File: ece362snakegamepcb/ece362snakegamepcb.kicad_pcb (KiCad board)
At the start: 2 copper layers, 52 x 71.5 mm, 49 parts, among them J1 USB_B_Micro, J2 Conn_02x26_Odd_Even, J3 Conn_02x26_Odd_Even, J4 SM03B-SRSS-TB, SW1 SW_Push, SW2 SW_Push, U1 RP2350_80QFN, U2 NCP1117-3.3_SOT223, U3 W25Q128JVS, U4 DNF, Y1 ABM8-272-T3

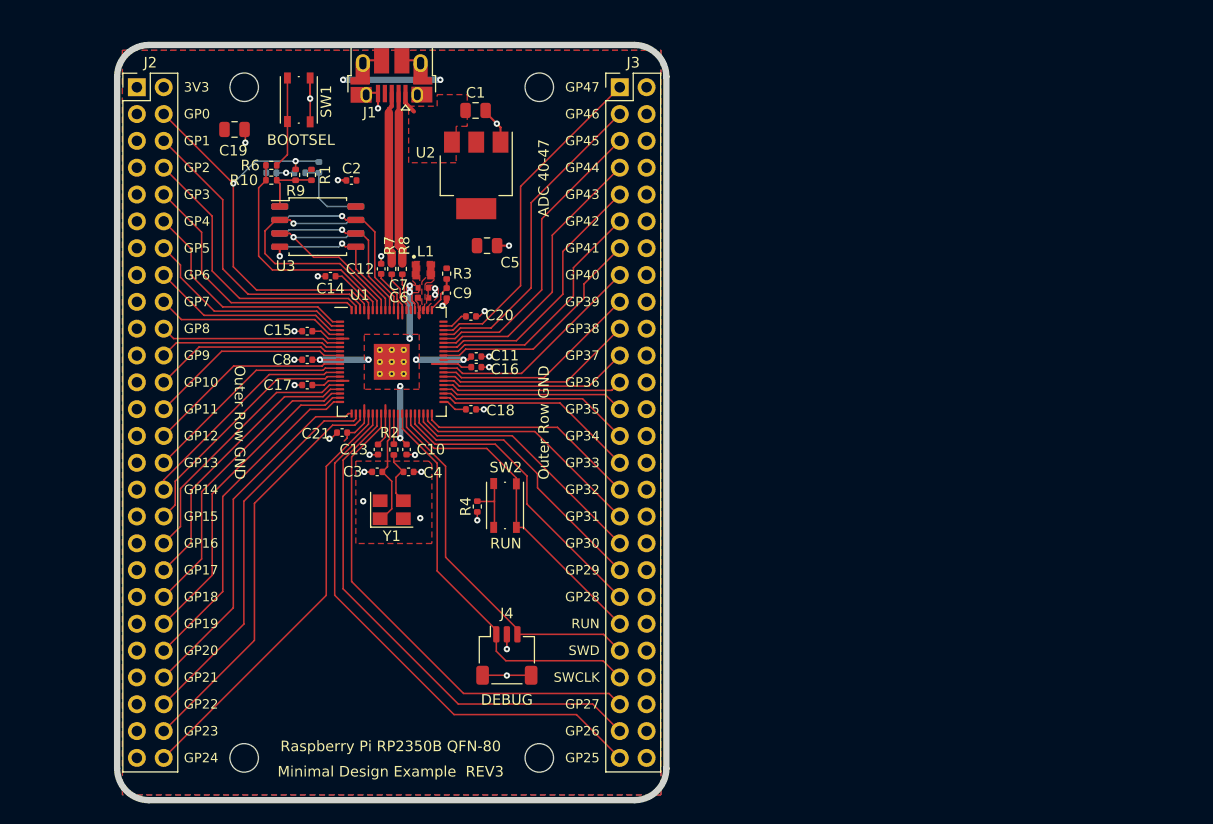
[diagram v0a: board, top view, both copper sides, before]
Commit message: Finished schematic and almost done with PCB layout. Removed autosave file and added several
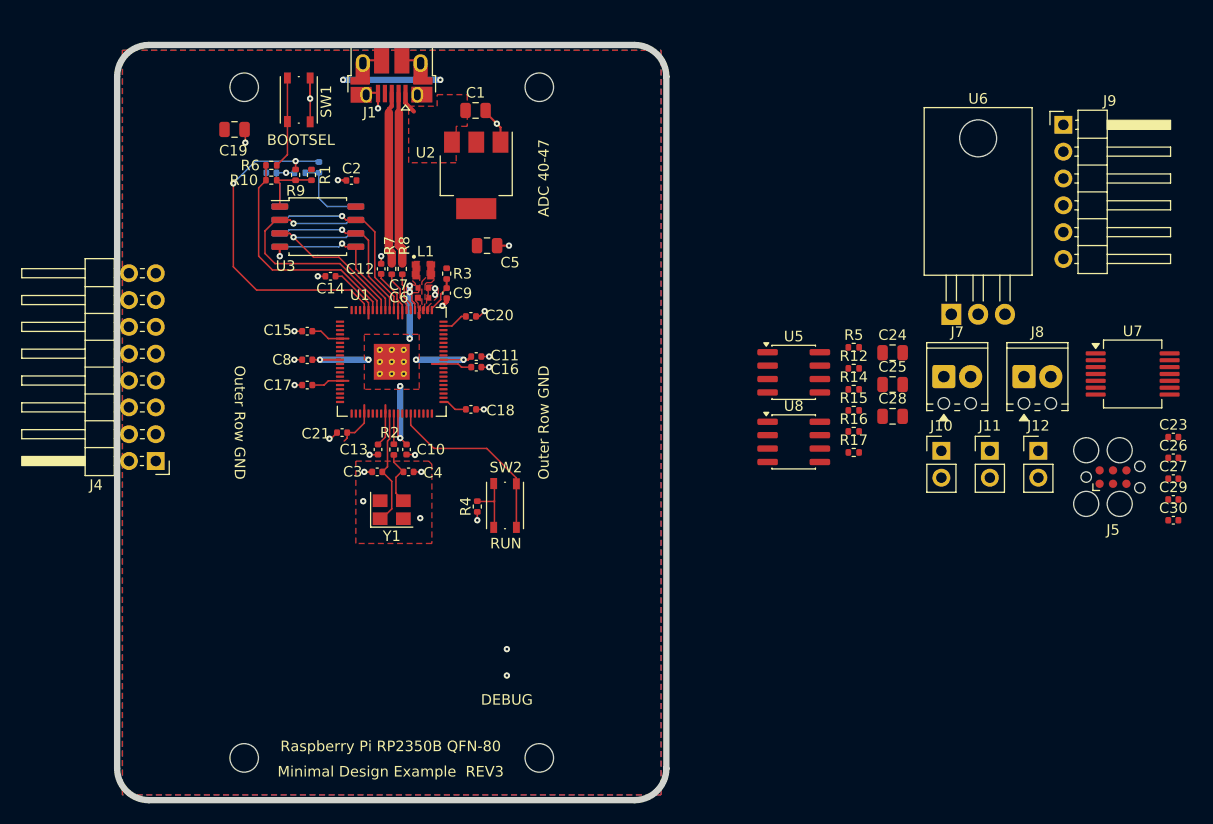
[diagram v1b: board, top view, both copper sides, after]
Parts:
- removed J2, J3: Conn_02x26_Odd_Even, Connector_PinHeader_2.54mm:PinHeader_2x26_P2.54mm_Vertical
- added C23: 100n, Capacitor_SMD:C_0402_1005Metric, F.Cu at (174.0, 107.1)
- added C24: 10u, Capacitor_SMD:C_0805_2012Metric, F.Cu at (147.4, 99.1)
- added C25: 10u, Capacitor_SMD:C_0805_2012Metric, F.Cu at (147.4, 102.2)
- added C26: 0.1u, Capacitor_SMD:C_0402_1005Metric, F.Cu at (174.0, 109.1)
- added C27: 100n, Capacitor_SMD:C_0402_1005Metric, F.Cu at (174.0, 111.1)
- added C28: 10u, Capacitor_SMD:C_0805_2012Metric, F.Cu at (147.4, 105.2)
- added C29: 250u, Capacitor_SMD:C_0402_1005Metric, F.Cu at (174.0, 113.0)
- added C30: 0.05u, Capacitor_SMD:C_0402_1005Metric, F.Cu at (174.0, 115.0)
- added J10: Conn_01x02_Pin, Connector_PinHeader_2.54mm:PinHeader_1x02_P2.54mm_Vertical, F.Cu at (152.0, 108.4)
- added J11: Conn_01x02_Pin, Connector_PinHeader_2.54mm:PinHeader_1x02_P2.54mm_Vertical, F.Cu at (156.6, 108.4)
- added J12: Conn_01x02_Pin, Connector_PinHeader_2.54mm:PinHeader_1x02_P2.54mm_Vertical, F.Cu at (161.2, 108.4)
- added J5: Conn_ARM_SWD_TagConnect_TC2030, Connector:Tag-Connect_TC2030-IDC-FP_2x03_P1.27mm_Vertical, F.Cu at (168.3, 110.9)
- added J7: Screw_Terminal_01x02, TerminalBlock_Phoenix:TerminalBlock_Phoenix_MPT-0,5-2-2.54_1x02_P2.54mm_Horizontal, F.Cu at (152.3, 101.4)
- added J8: Screw_Terminal_01x02, TerminalBlock_Phoenix:TerminalBlock_Phoenix_MPT-0,5-2-2.54_1x02_P2.54mm_Horizontal, F.Cu at (159.9, 101.4)
- added J9: Conn_01x06_Pin, Connector_PinHeader_2.54mm:PinHeader_1x06_P2.54mm_Horizontal, F.Cu at (163.6, 77.6)
- added R12: 4.7k, Resistor_SMD:R_0402_1005Metric, F.Cu at (143.7, 100.6)
- added R14: 4.7k, Resistor_SMD:R_0402_1005Metric, F.Cu at (143.7, 102.6)
- added R15: 4.7k, Resistor_SMD:R_0402_1005Metric, F.Cu at (143.7, 104.6)
- added R16: 4.7k, Resistor_SMD:R_0402_1005Metric, F.Cu at (143.7, 106.6)
- added R17: 1k, Resistor_SMD:R_0402_1005Metric, F.Cu at (143.7, 108.6)
- added R5: 10k, Resistor_SMD:R_0402_1005Metric, F.Cu at (143.7, 98.6)
- added U5: 24AA025E-SN, Package_SO:SOIC-8_3.9x4.9mm_P1.27mm, F.Cu at (138.1, 101.0)
- added U6: LM1084-5.0, Package_TO_SOT_THT:TO-220-3_Horizontal_TabDown, F.Cu at (153.0, 95.5)
- added U7: LM324, Package_SO:SSOP-14_5.3x6.2mm_P0.65mm, F.Cu at (170.2, 101.2)
- added U8: LM386, Package_SO:SOIC-8_3.9x4.9mm_P1.27mm, F.Cu at (138.1, 107.6)
- J4: value SM03B-SRSS-TB -> Conn_02x08_Counter_Clockwise; footprint Connector_JST:JST_SH_SM03B-SRSS-TB_1x03-1MP_P1.00mm_Horizontal -> Connector_PinHeader_2.54mm:PinHeader_2x08_P2.54mm_Horizontal
- moved J4 38.0 mm to (77.7, 109.4), turned to 180 degrees
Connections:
- J4 pad 1: /SWCLK -> /GPIO8
- J4 pad 2: GND -> /GPIO10
- J4 pad 3: /SWD -> /GPIO11
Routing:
- net /GPIO25: track 52.1 -> 0.00 mm
- net /GPIO26: track 49.7 -> 0.00 mm
- net /GPIO27: track 47.3 -> 0.00 mm
- net /GPIO24: track 40.6 -> 0.00 mm
- net /GPIO23: track 39.0 -> 0.00 mm
- net /SWCLK: track 38.9 -> 0.00 mm
- net /GPIO22: track 36.7 -> 0.00 mm
- net /SWD: track 35.6 -> 0.00 mm
- net /GPIO21: track 34.2 -> 0.00 mm
- net /GPIO47_ADC7: track 31.7 -> 0.00 mm
- net /GPIO20: track 31.7 -> 0.00 mm
- net /GPIO19: track 30.1 -> 0.00 mm
- net /GPIO46_ADC6: track 30.1 -> 0.00 mm
- net /GPIO1: track 29.4 -> 0.00 mm
- net /GPIO28: track 28.7 -> 0.00 mm
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- added copper zone on In1.Cu, net GND
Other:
- copper layers 2 -> 4
- board text removed: "3V3"
- board text removed: "GP0"
- board text removed: "GP1"
- board text removed: "GP10"
- board text removed: "GP11"
- board text removed: "GP12"
- board text removed: "GP13"
- board text removed: "GP14"
- board text removed: "GP15"
- board text removed: "GP16"
- board text removed: "GP17"
- board text removed: "GP18"
- board text removed: "GP19"
- board text removed: "GP2"
- board text removed: "GP20"
- board text removed: "GP21"
- board text removed: "GP22"
- board text removed: "GP23"
- board text removed: "GP24"
- board text removed: "GP25"
- board text removed: "GP26"
- board text removed: "GP27"
- board text removed: "GP28"
- board text removed: "GP29"
- board text removed: "GP3"
- board text removed: "GP30"
- board text removed: "GP31"
- board text removed: "GP32"
- board text removed: "GP33"
- board text removed: "GP34"
- board text removed: "GP35"
- board text removed: "GP36"
- board text removed: "GP37"
- board text removed: "GP38"
- board text removed: "GP39"
- board text removed: "GP4"
- board text removed: "GP40"
- board text removed: "GP41"
- board text removed: "GP42"
- board text removed: "GP43"
- board text removed: "GP44"
- board text removed: "GP45"
- board text removed: "GP46"
- board text removed: "GP47"
- board text removed: "GP5"
- board text removed: "GP6"
- board text removed: "GP7"
- board text removed: "GP8"
- board text removed: "GP9"
- board text removed: "SWCLK"
- board text removed: "SWD"

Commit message: Finished pcb layout, but need to fix DRC erros
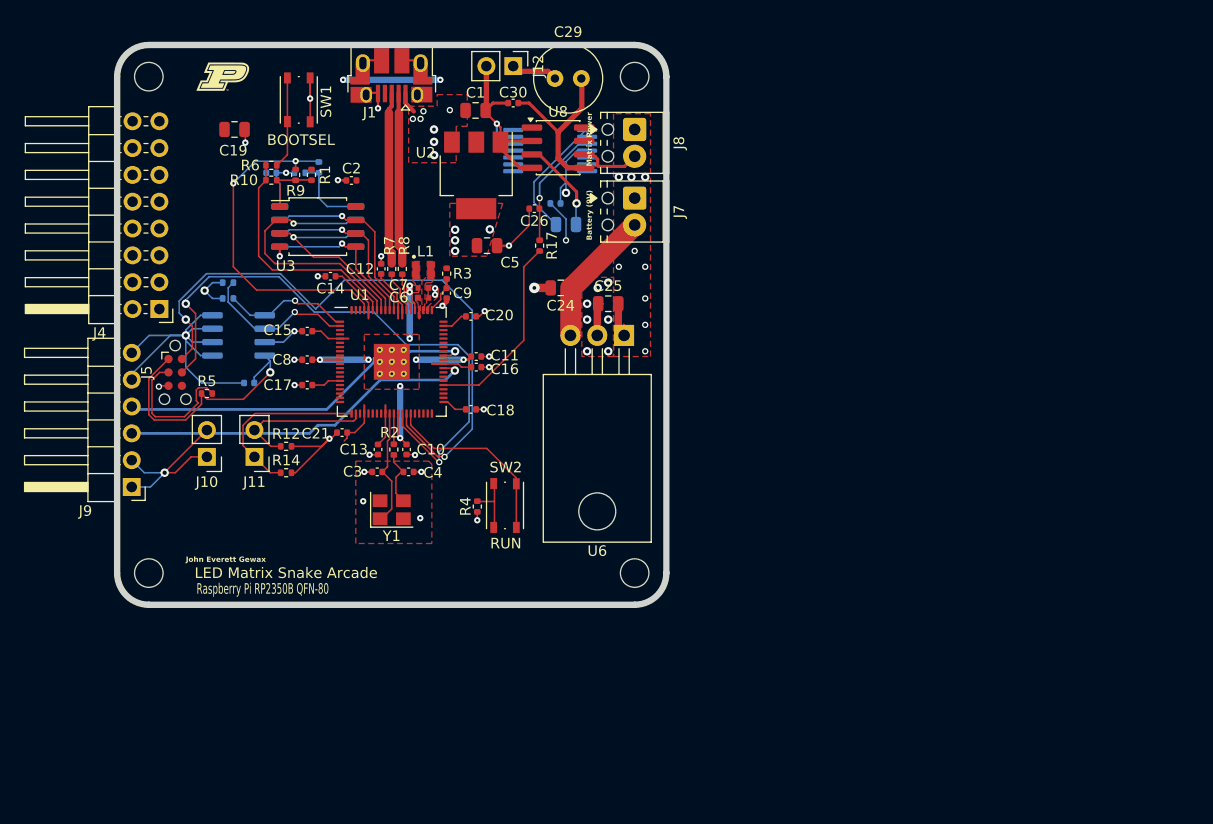
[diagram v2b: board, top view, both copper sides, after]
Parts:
- added G***: LOGO, LOGO, F.Cu at (84.0, 73.0)
- C23, C27, C28, R15, R16, U5, U7: moved to B.Cu
- C29: footprint Capacitor_SMD:C_0402_1005Metric -> Capacitor_THT:C_Radial_D6.3mm_H5.0mm_P2.50mm
- J5: footprint Connector:Tag-Connect_TC2030-IDC-FP_2x03_P1.27mm_Vertical -> Connector:Tag-Connect_TC2030-IDC-NL_2x03_P1.27mm_Vertical
- moved J9 94.6 mm to (75.4, 111.8), turned to 180 degrees
- moved J5 89.3 mm to (79.5, 101.0), turned to -90 degrees
- moved C23 87.6 mm to (86.5, 102.0), turned to 180 degrees
- moved C30 73.9 mm to (111.5, 75.5), turned to 180 degrees
- moved C29 70.8 mm to (115.5, 73.2)
- moved J11 69.6 mm to (87.0, 109.0), turned to 180 degrees
- moved J10 69.5 mm to (82.5, 109.0), turned to 180 degrees
- moved C26 64.9 mm to (113.5, 85.5), turned to 180 degrees
- moved C27 64.0 mm to (115.5, 85.0), turned to 180 degrees
- moved J12 61.6 mm to (111.5, 72.0), turned to -90 degrees
- moved R5 61.4 mm to (82.5, 103.0)
- moved R16 60.6 mm to (84.5, 94.0)
- moved R15 60.5 mm to (84.5, 92.5)
- moved U7 59.1 mm to (115.0, 80.0), turned to 180 degrees
- moved R14 54.3 mm to (90.0, 110.5)
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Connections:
- net Net-(J7-Pin_2) renamed +9V
- C23 pad 1: +3.3V -> +3V3
- J10 pad 1: +3.3V -> +3V3
- J10 pad 2: +3.3V -> +3V3
- J9 pad 1: +3.3V -> +3V3
- J9 pad 2: +3.3V -> +3V3
- R15 pad 1: +3.3V -> +3V3
- R16 pad 1: +3.3V -> +3V3
- U5 pad 8: +3.3V -> +3V3
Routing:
- net GND: track 32.8 -> 110.8 mm, vias 29 -> 40
- net /SWD: track 0.00 -> 59.9 mm, vias 0 -> 2
- net /SWCLK: track 0.00 -> 55.9 mm, vias 0 -> 2
- net +3V3: track 52.9 -> 98.9 mm, vias 3 -> 10
- net /GPIO41_ADC1: track 0.00 -> 34.5 mm, vias 0 -> 1
- net /GPIO40_ADC0: track 0.00 -> 34.2 mm, vias 0 -> 1
- net /GPIO36: track 0.00 -> 18.4 mm
- net VBUS: track 2.11 -> 20.2 mm, vias 0 -> 15
- net /GPIO21: track 0.00 -> 17.3 mm
- net Net-(C29-Pad2): track 0.00 -> 16.2 mm
- net /GPIO5: track 0.00 -> 14.9 mm, vias 0 -> 1
- net /GPIO22: track 0.00 -> 13.7 mm
- net Net-(J5-~{RESET}): track 0.00 -> 13.2 mm
- net +9V: track 0.00 -> 13.0 mm
- net Net-(U7A--): track 0.00 -> 12.6 mm
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- added copper zone on In2.Cu, net +3V3
- added copper zone on In2.Cu, net VBUS
- removed copper zone on B.Cu, net GND
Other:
- board size 52 x 71.5 mm -> 52 x 53 mm
- board text added: "Battery (9V)"
- board text added: "John Everett Gewax"
- board text added: "LED Matrix Snake Arcade"
- board text added: "Matrix Power"
- board text removed: "ADC 40-47"
- board text removed: "DEBUG"
- board text removed: "Minimal Design Example REV3"
- board text removed: "Outer Row GND"

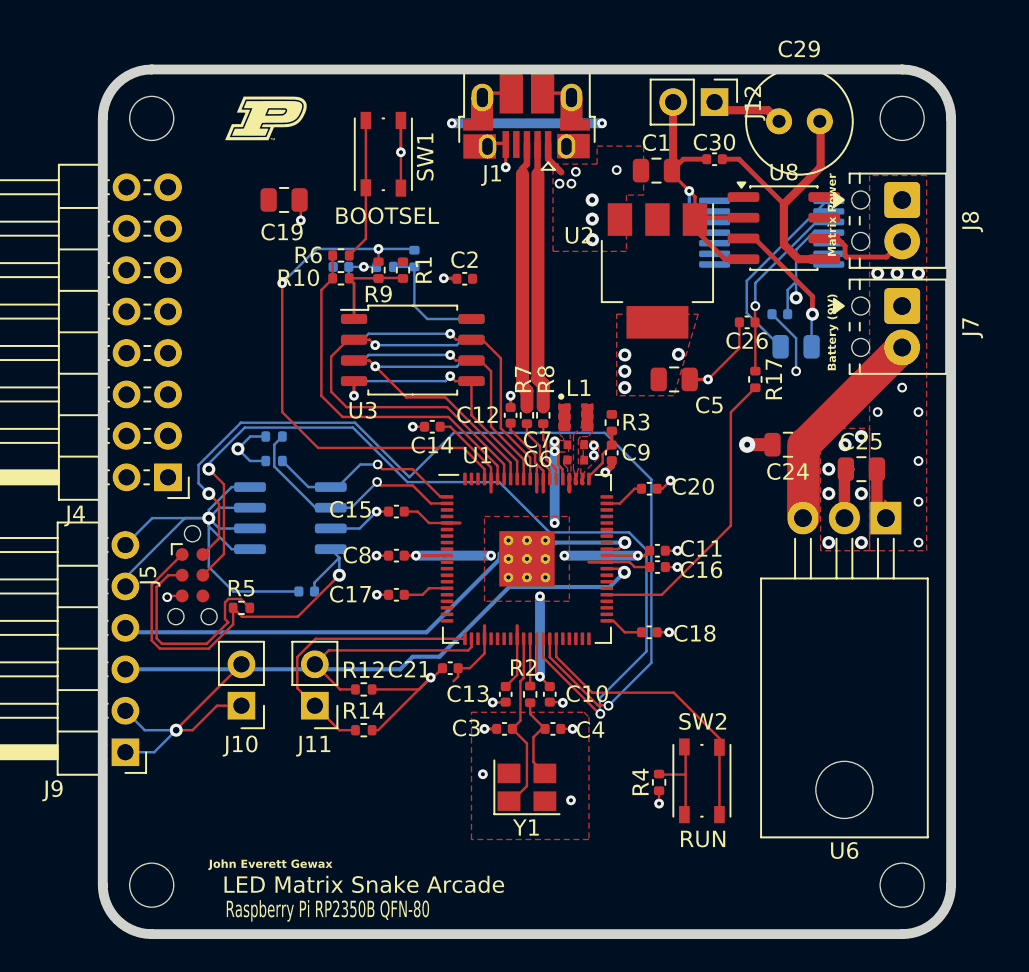
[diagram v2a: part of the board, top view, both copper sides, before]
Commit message: done except some drc errors (mostly silkscreen):
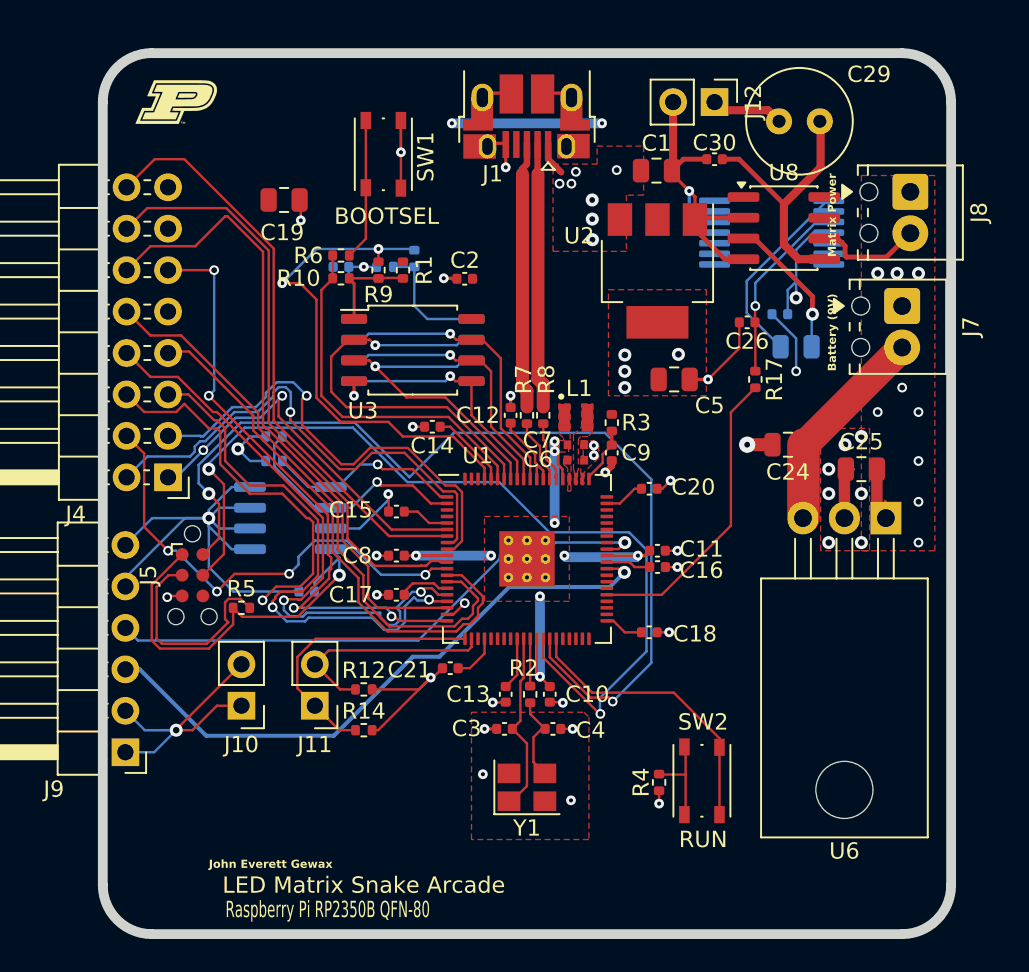
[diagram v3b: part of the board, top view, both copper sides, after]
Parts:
- removed H1, H2, H3, H4: MountingHole, MountingHole:MountingHole_2.7mm_M2.5
- moved G*** 5.59 mm to (78.5, 72.0)
- moved J8 0.71 mm to (123.5, 77.5)
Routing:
- net /GPIO18: track 0.00 -> 39.7 mm
- net /GPIO20: track 0.00 -> 37.8 mm, vias 0 -> 4
- net /GPIO12: track 0.00 -> 36.9 mm
- net /GPIO9: track 0.00 -> 36.1 mm
- net /GPIO16: track 0.00 -> 36.1 mm, vias 0 -> 2
- net /GPIO15: track 0.00 -> 35.9 mm
- net /GPIO17: track 0.00 -> 33.8 mm, vias 0 -> 2
- net /GPIO14: track 0.00 -> 33.5 mm
- net /GPIO10: track 0.00 -> 30.9 mm, vias 0 -> 1
- net /GPIO13: track 0.00 -> 28.8 mm, vias 0 -> 4
- net /GPIO11: track 0.00 -> 28.8 mm, vias 0 -> 1
- net /GPIO19: track 0.00 -> 24.6 mm, vias 0 -> 2
- net /GPIO8: track 0.00 -> 23.6 mm, vias 0 -> 2
- net +3V3: track 98.9 -> 91.7 mm
- net /GPIO40_ADC0: track 34.2 -> 37.6 mm
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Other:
- board size 52 x 53 mm -> 52 x 54 mm
